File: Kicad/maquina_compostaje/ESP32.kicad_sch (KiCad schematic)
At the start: 11 parts, among them J1 Conn_01x06, J2 Conn_01x09, SW1 1825910-6, SW2 1825910-6, U1 ESP32-WROOM-32

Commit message: inicio del ruteo
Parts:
- removed J2: Conn_01x09, Connector_JST:JST_EH_B9B-EH-A_1x09_P2.50mm_Vertical, symbol Connector_Generic:Conn_01x09
- added C17: 0.1uF, Capacitor_SMD:C_1206_3216Metric_Pad1.33x1.80mm_HandSolder, symbol Device:C_Small
- added C18: 10uF, Capacitor_SMD:C_1206_3216Metric_Pad1.33x1.80mm_HandSolder, symbol Device:C_Small
- added J2: Conenctor_GPIO, Connector_JST:JST_EH_B5B-EH-A_1x05_P2.50mm_Vertical, symbol Connector:Screw_Terminal_01x05
- R2, R3: value 470 -> 4.7K
- SW1: value 1825910-6 -> RESET; footprint 1825910-6:SW_1825910-6-4 -> w_switch:smd_push2
- SW2: value 1825910-6 -> BOOT; footprint 1825910-6:SW_1825910-6-4 -> w_switch:smd_push2
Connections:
- net 3.3V: now also C17.2, C18.1
- net GND: now also C17.1, C18.2
- net RX: now also U1.35 (TXD0/IO1); no longer R2.2
- net SCL: now also R2.1
- net SDA: now also R3.1
- net TX: now also U1.34 (RXD0/IO3); no longer R3.2
- net gpio16: now also J2.2 (Pin_2)
- net gpio17: now also J2.3 (Pin_3)
- net gpio2: now also J2.1 (Pin_1)
- net gpio23: now also J2.4 (Pin_4)
- net gpio35: now also J2.5 (Pin_5)
- net gpio33 renamed EN_1B
- net gpio34 renamed EN_2B
- net gpio4 renamed EN_1A
- net gpio5 renamed EN_2A
- new net +3.3V: R2.2, R3.2

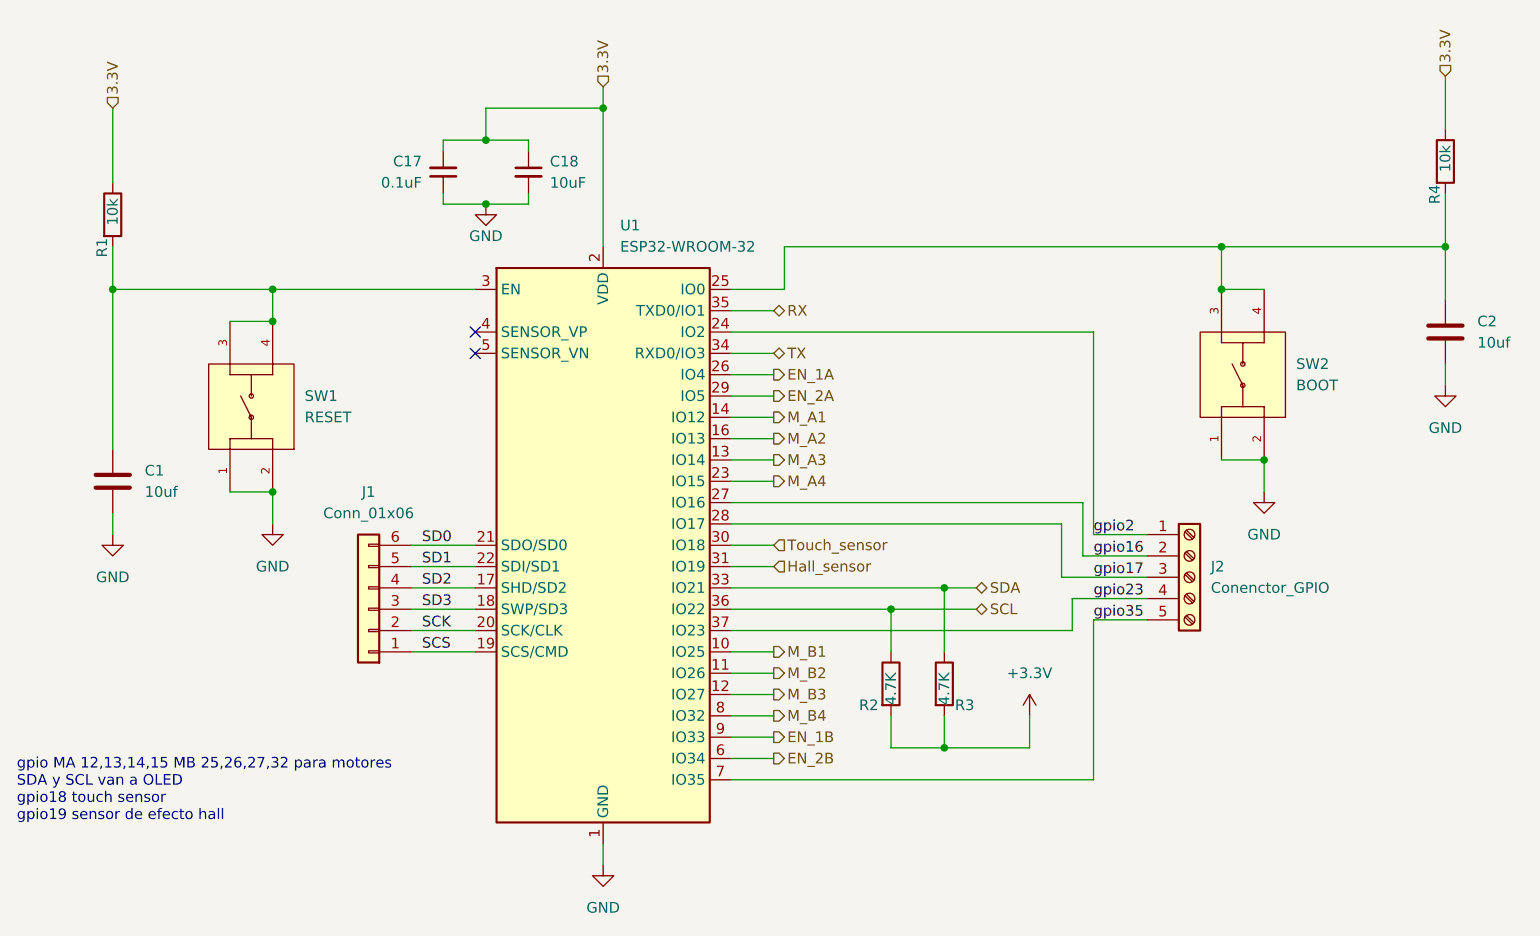
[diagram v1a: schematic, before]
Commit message: se agregaron componentes en la parte inferior de la placa
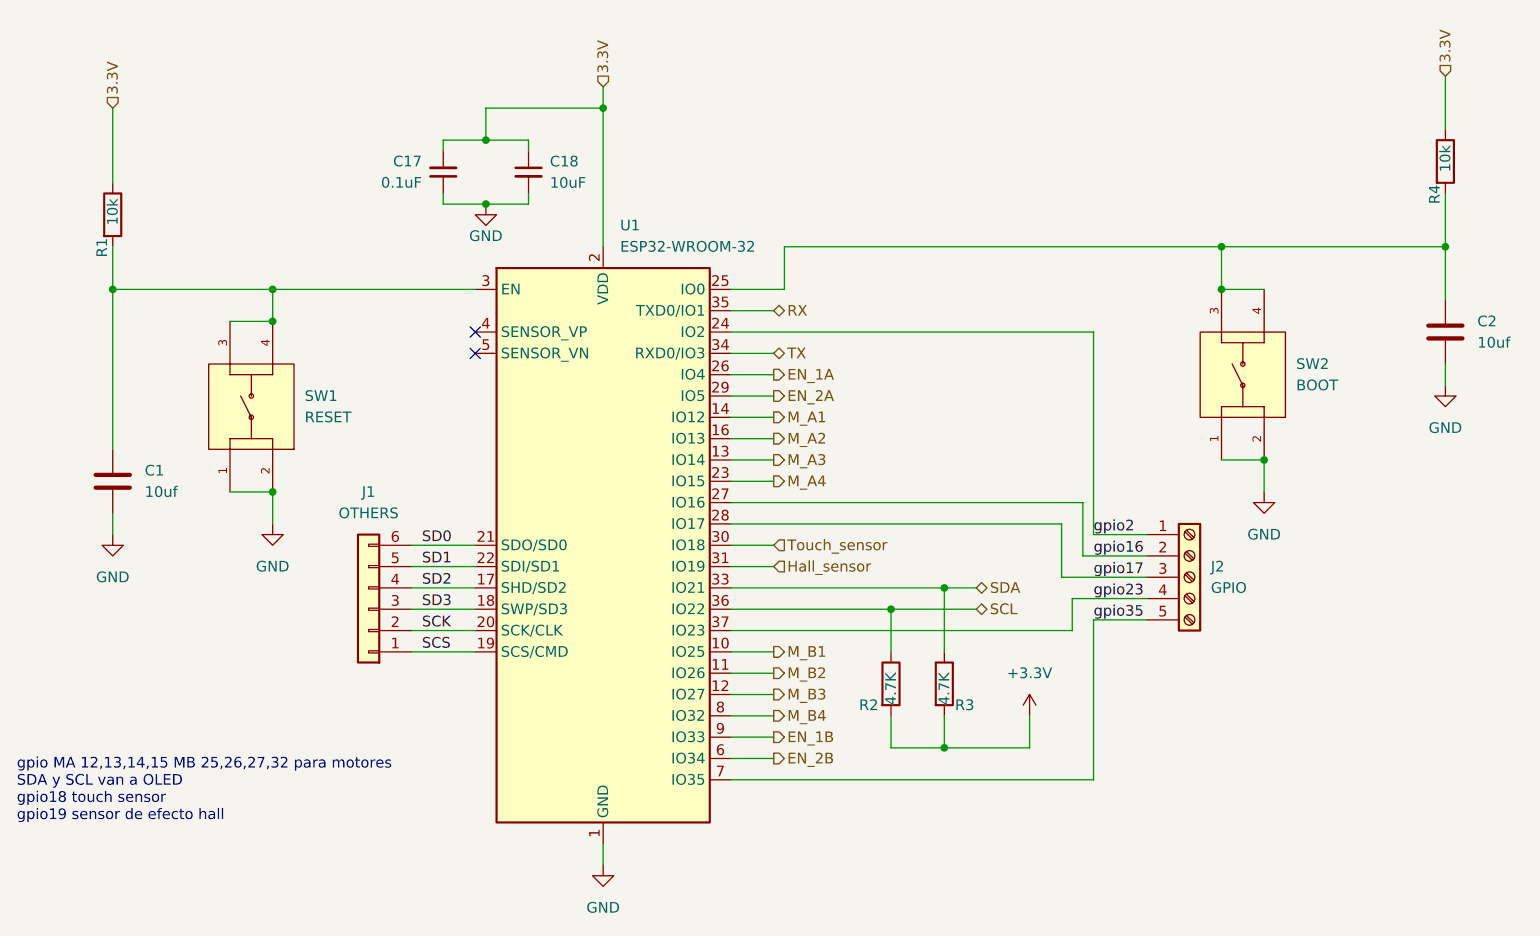
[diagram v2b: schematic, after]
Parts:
- J1: value Conn_01x06 -> OTHERS
- J2: value Conenctor_GPIO -> GPIO
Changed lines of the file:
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@@
       (effects (font (size 1.27 1.27)) (justify left))
     )
-    (property "Value" "Conenctor_GPIO" (id 1) (at 226.06 109.2199 0)
+    (property "Value" "GPIO" (id 1) (at 226.06 109.2199 0)
       (effects (font (size 1.27 1.27)) (justify left))
     )
@@
     (in_bom yes) (on_board yes) (fields_autoplaced)
     (property "Reference" "J1" (id 0) (at 125.73 97.79 0))
-    (property "Value" "Conn_01x06" (id 1) (at 125.73 100.33 0))
+    (property "Value" "OTHERS" (id 1) (at 125.73 100.33 0))
     (property "Footprint" "Connector_JST:JST_EH_B6B-EH-A_1x06_P2.50mm_Vertical" (id 2) (at 125.73 111.76 0)
       (effects (font (size 1.27 1.27)) hide)
